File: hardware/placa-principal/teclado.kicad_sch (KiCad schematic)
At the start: 11 parts, among them CN2 Membranas do teclado, U16 74LS273, U22 74LS244

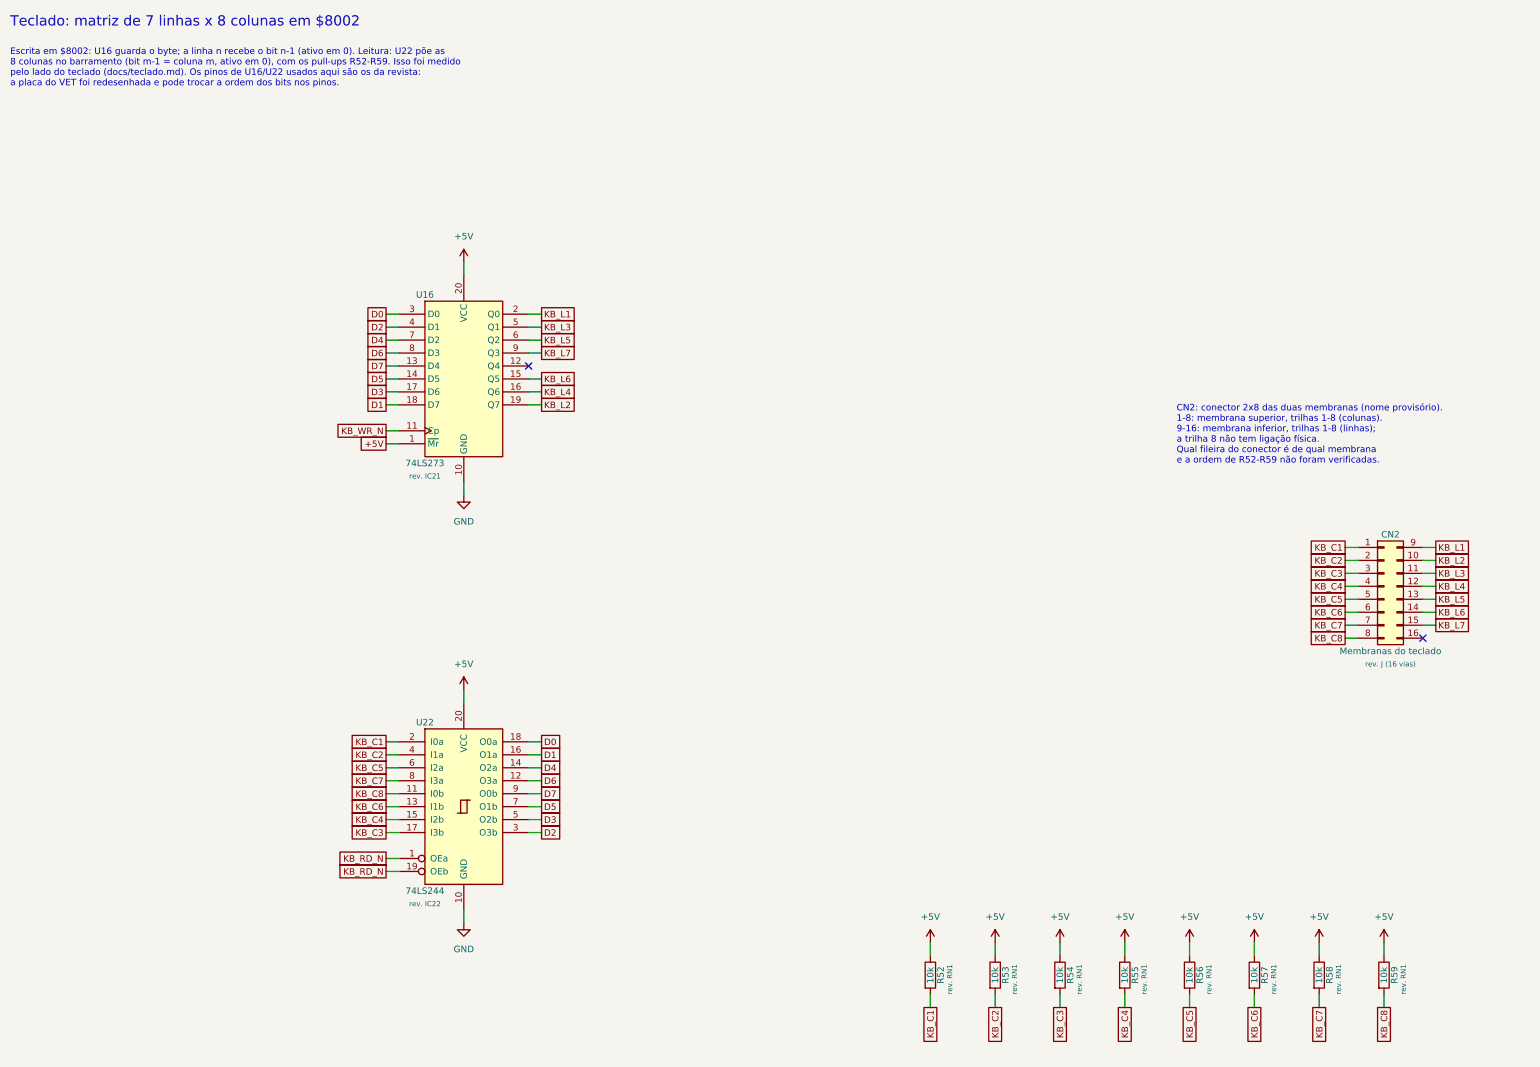
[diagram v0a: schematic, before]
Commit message: Esquema: placa da fonte e medidas do teclado, pull-ups e /OE
- Folha Fonte (fonte.kicad_sch), levantada das fotos dos dois lados da
  placa: ponte com derivação central, 7805, 7812, 7905 com bomba de carga,
  backup da RAM (+3V_BAT) e conector de saída. Explica os ~11 V no +5 V
  quando a fonte é testada sem carga.
- Teclado medido: U16 (74LS273) e U22 (74LS244) ligam D0-D7 com os mesmos
  pinos da revista (Fig. 14), e o /CLR do U16 vai ao +5 V. O conector das
  membranas é o CN3: pino 1 embaixo à esquerda, ímpares = membrana inferior
  (linhas, U16), pares = superior (colunas, U22 e R52-R59), tudo medido.
- CN2 = entrada da fonte na placa principal.
- R30 é o pull-up do /HALT e R29 o do /IRQ; /OE da EPROM e das duas
  µPD41416 no GND (medidos).
- Roteiro de continuidade: 38 redes medidas, 6 parciais, 39 só da revista.
  Docs (hardware, teclado, origem) atualizados.

Co-Authored-By: Claude Opus 5.5 <noreply@anthropic.com>
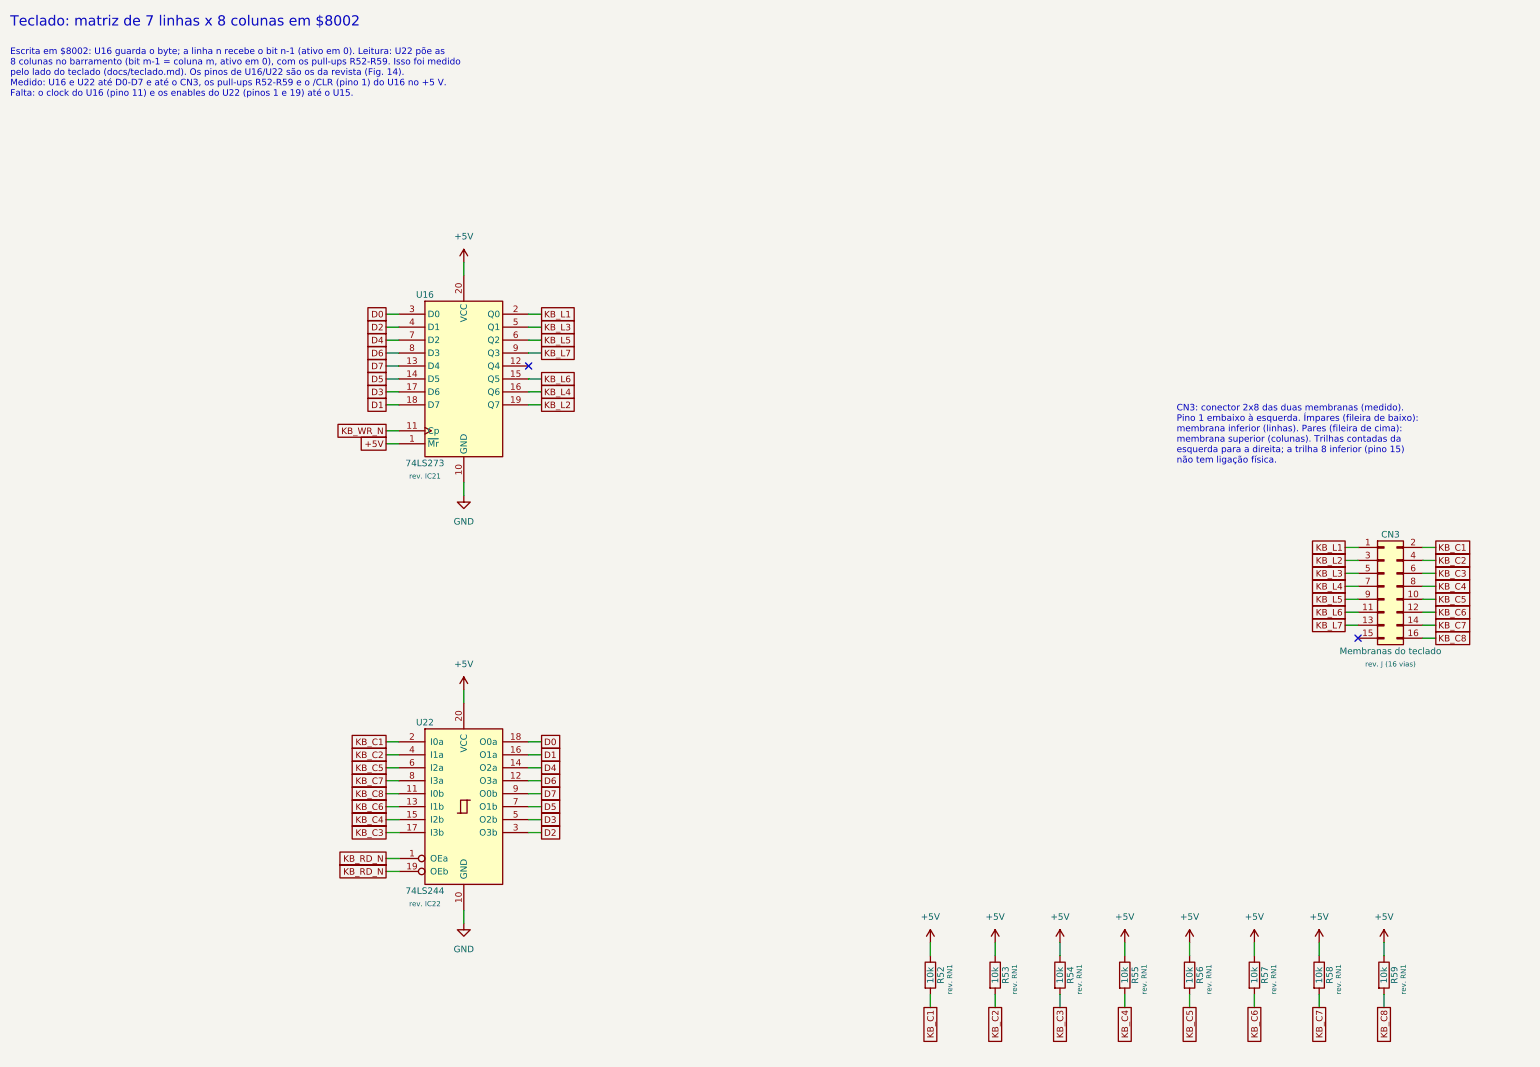
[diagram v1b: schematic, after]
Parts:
- removed CN2: Membranas do teclado, Connector_PinHeader_2.54mm:PinHeader_2x08_P2.54mm_Vertical, symbol Connector_Generic:Conn_02x08_Top_Bottom
- added CN3: Membranas do teclado, Connector_PinHeader_2.54mm:PinHeader_2x08_P2.54mm_Vertical, symbol Connector_Generic:Conn_02x08_Odd_Even
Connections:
- net KB_C1: now also CN3.2 (Pin_2)
- net KB_C2: now also CN3.4 (Pin_4)
- net KB_C3: now also CN3.6 (Pin_6)
- net KB_C4: now also CN3.8 (Pin_8)
- net KB_C5: now also CN3.10 (Pin_10)
- net KB_C6: now also CN3.12 (Pin_12)
- net KB_C7: now also CN3.14 (Pin_14)
- net KB_C8: now also CN3.16 (Pin_16)
- net KB_L1: now also CN3.1 (Pin_1)
- net KB_L2: now also CN3.3 (Pin_3)
- net KB_L3: now also CN3.5 (Pin_5)
- net KB_L4: now also CN3.7 (Pin_7)
- net KB_L5: now also CN3.9 (Pin_9)
- net KB_L6: now also CN3.11 (Pin_11)
- net KB_L7: now also CN3.13 (Pin_13)
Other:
- note added: "CN3: conector 2x8 das duas membranas (medido). Pino 1 embaixo à esquerda. Ímpares (fileira de baixo): membrana inferior (linhas). Pares (fileira de cima): membrana superior (colunas). Trilhas contadas da esquerda para a direita; a trilha 8 inferior (pino 15) não tem ligação física."
- note added: "Escrita em $8002: U16 guarda o byte; a linha n recebe o bit n-1 (ativo em 0). Leitura: U22 põe as 8 colunas no barramento (bit m-1 = coluna m, ativo em 0), com os pull-ups R52-R59. Isso foi medido pelo lado do teclado (docs/teclado.md). Os pinos de U16/U22 são os da revista (Fig. 14). Medido: U16 e U22 até D0-D7 e até o CN3, os pull-ups R52-R59 e o /CLR (pino 1) do U16 no +5 V. Falta: o clock do 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"
- note removed: "CN2: conector 2x8 das duas membranas (nome provisório). 1-8: membrana superior, trilhas 1-8 (colunas). 9-16: membrana inferior, trilhas 1-8 (linhas); a trilha 8 não tem ligação física. Qual fileira do conector é de qual membrana e a ordem de R52-R59 não foram verificadas."
- note removed: "Escrita em $8002: U16 guarda o byte; a linha n recebe o bit n-1 (ativo em 0). Leitura: U22 põe as 8 colunas no barramento (bit m-1 = coluna m, ativo em 0), com os pull-ups R52-R59. Isso foi medido pelo lado do teclado (docs/teclado.md). Os pinos de U16/U22 usados aqui são os da revista: a placa do VET foi redesenhada e pode trocar a ordem dos bits nos pinos."

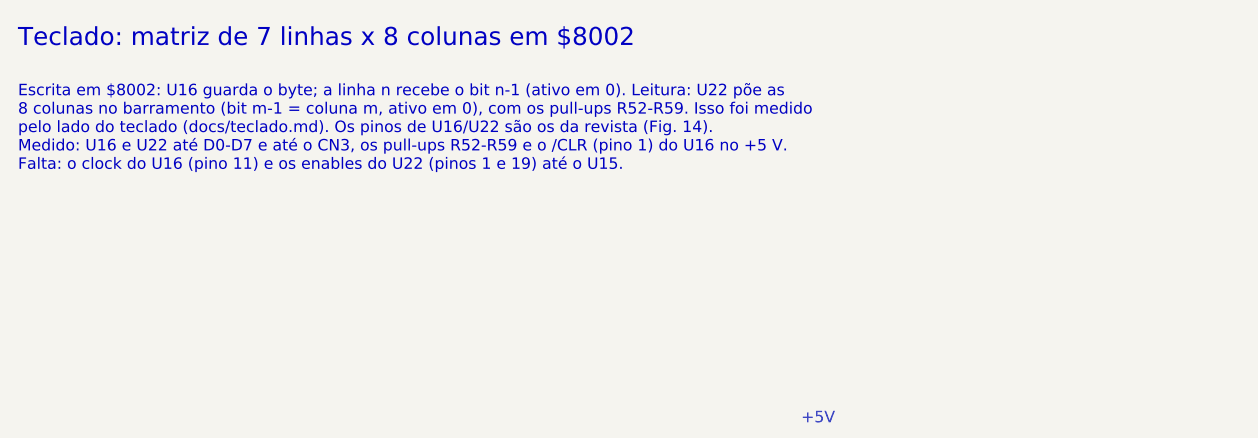
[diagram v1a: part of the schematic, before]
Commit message: Placa principal: CN2 e seleção do teclado medidos, fonte consertada
- CN2 medido: ordem inversa da do CN201 da fonte (GND no pino 1, -5 V no
  pino 5). Esquema, roteiro e docs corrigidos.
- Seleção do teclado medida: U15 pino 10 no clock do U16 e pino 9 nos
  enables do U22, como na revista. Roteiro: 40 redes medidas, 6 parciais,
  37 só da revista.
- Fonte: D210 identificado (1N4148, estava aberto); trocados D207, D208,
  D210, C203, C205 e R201. Tabela com as tensões medidas depois do
  conserto e carga de teste corrigida para 47 ohms (a de 100 ohms puxa
  menos que os ~60 mA do R201). O VET liga e mostra a abertura.

Trabalho feito em outra sessão, commitado sem alterações.

Co-Authored-By: Claude Opus 5.5 <noreply@anthropic.com>
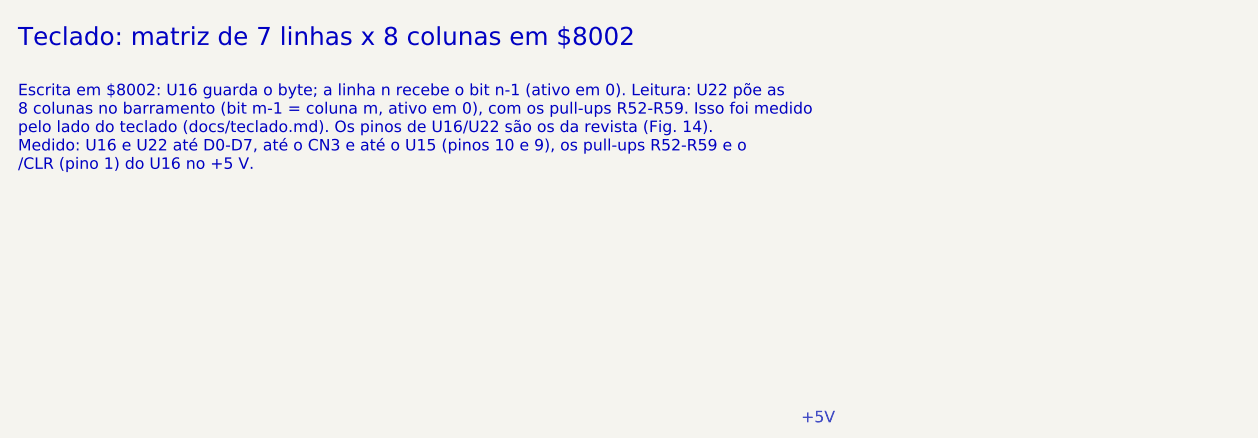
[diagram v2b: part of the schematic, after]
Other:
- note added: "Escrita em $8002: U16 guarda o byte; a linha n recebe o bit n-1 (ativo em 0). Leitura: U22 põe as 8 colunas no barramento (bit m-1 = coluna m, ativo em 0), com os pull-ups R52-R59. Isso foi medido pelo lado do teclado (docs/teclado.md). Os pinos de U16/U22 são os da revista (Fig. 14). Medido: U16 e U22 até D0-D7, até o CN3 e até o U15 (pinos 10 e 9), os pull-ups R52-R59 e o /CLR (pino 1) do U16 n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"
- note removed: "Escrita em $8002: U16 guarda o byte; a linha n recebe o bit n-1 (ativo em 0). Leitura: U22 põe as 8 colunas no barramento (bit m-1 = coluna m, ativo em 0), com os pull-ups R52-R59. Isso foi medido pelo lado do teclado (docs/teclado.md). Os pinos de U16/U22 são os da revista (Fig. 14). Medido: U16 e U22 até D0-D7 e até o CN3, os pull-ups R52-R59 e o /CLR (pino 1) do U16 no +5 V. Falta: o clock do 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"
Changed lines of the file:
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@@
 		)
 	)
-	(text "Escrita em $8002: U16 guarda o byte; a linha n recebe o bit n-1 (ativo em 0). Leitura: U22 põe as\n8 colunas no barramento (bit m-1 = coluna m, ativo em 0), com os pull-ups R52-R59. Isso foi medido\npelo lado do teclado (docs/teclado.md). Os pinos de U16/U22 são os da revista (Fig. 14).\nMedido: U16 e U22 até D0-D7 e até o CN3, os pull-ups R52-R59 e o /CLR (pino 1) do U16 no +5 V.\nFalta: o clock do U16 (pino 11) e os enables do U22 (pinos 1 e 19) até o U15."
+	(text "Escrita em $8002: U16 guarda o byte; a linha n recebe o bit n-1 (ativo em 0). Leitura: U22 põe as\n8 colunas no barramento (bit m-1 = coluna m, ativo em 0), com os pull-ups R52-R59. Isso foi medido\npelo lado do teclado (docs/teclado.md). Os pinos de U16/U22 são os da revista (Fig. 14).\nMedido: U16 e U22 até D0-D7, até o CN3 e até o U15 (pinos 10 e 9), os pull-ups R52-R59 e o\n/CLR (pino 1) do U16 no +5 V."
 		(exclude_from_sim no)
 		(at 25.4 26.67 0)
